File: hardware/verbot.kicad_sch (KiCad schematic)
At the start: 6 parts, among them J1 Raspberry Pi Zero 2 W, J2 5V USB power bank, M1 Pimoroni OnOff SHIM, M2 DRV8833 carrier, M3 Verbot 3V motor

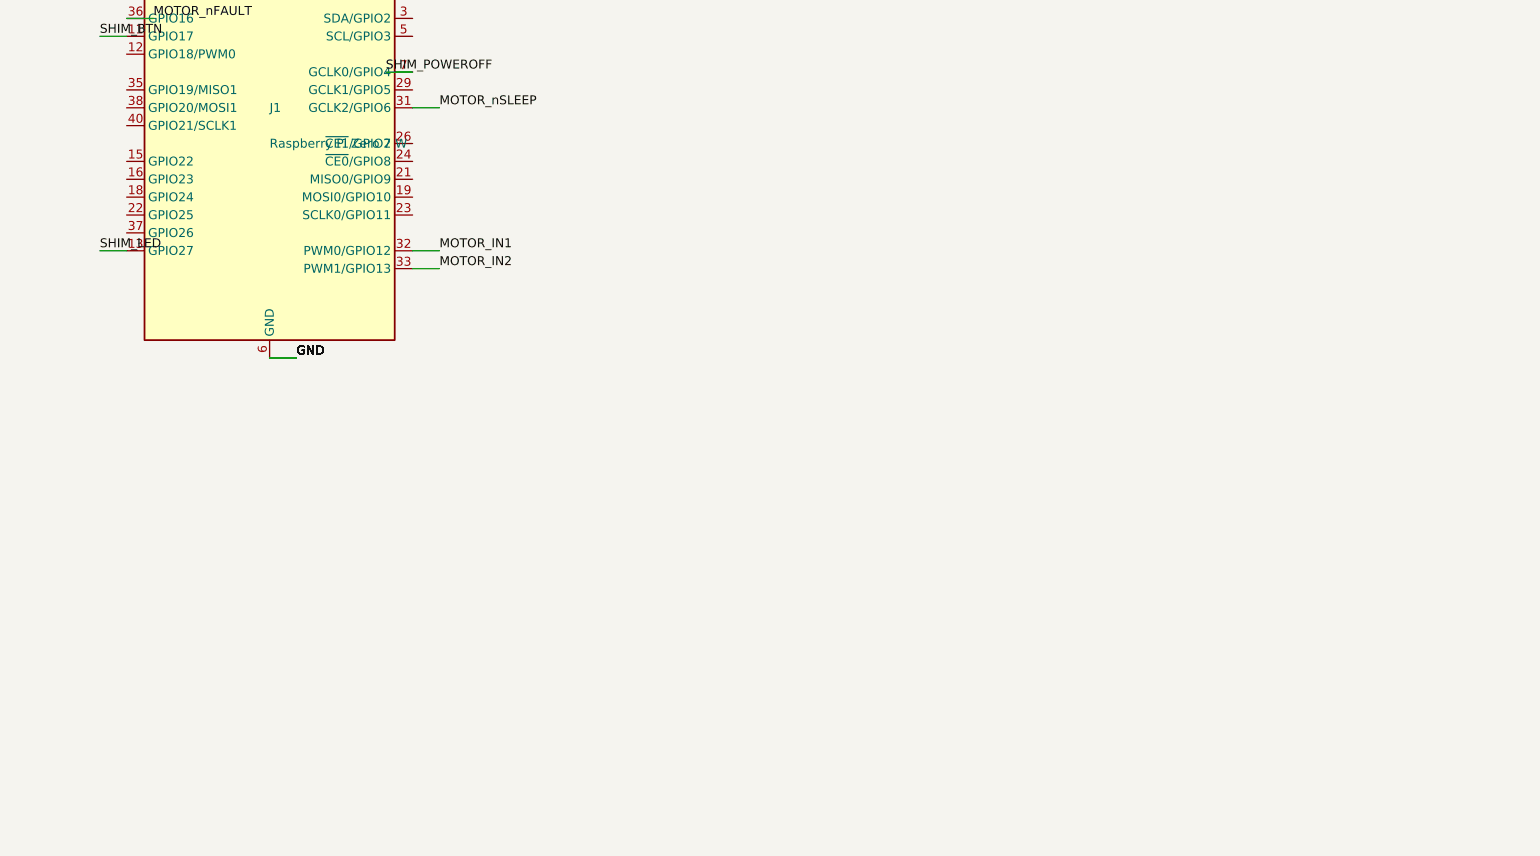
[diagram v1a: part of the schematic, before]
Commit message: feat(hardware): interrogation switch bank and limit switches
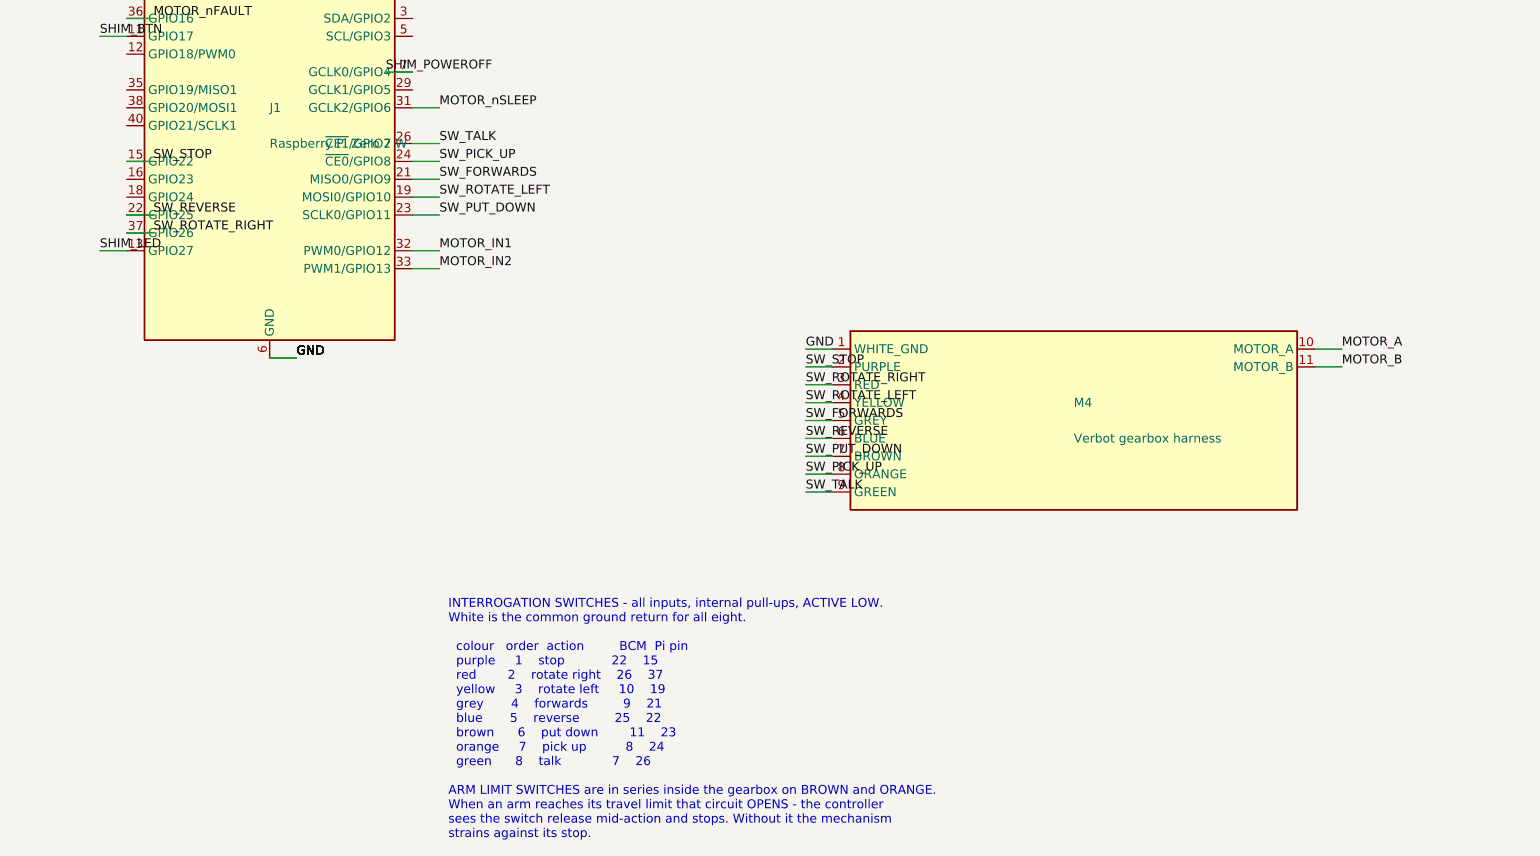
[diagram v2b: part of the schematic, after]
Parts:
- added M4: Verbot gearbox harness, symbol verbot:Verbot_Gearbox
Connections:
- net GND: now also M4.1 (WHITE_GND)
- net MOTOR_A: now also M4.10 (MOTOR_A)
- net MOTOR_B: now also M4.11 (MOTOR_B)
- net SW_STOP: now reaches J1.15 (GPIO22)
- net SW_STOP: now also M4.2 (PURPLE)
- net SW_ROTATE_LEFT: now reaches J1.19 (MOSI0/GPIO10)
- net SW_ROTATE_LEFT: now also M4.4 (YELLOW)
- net SW_FORWARDS: now reaches J1.21 (MISO0/GPIO9)
- net SW_FORWARDS: now also M4.5 (GREY)
- net SW_REVERSE: now reaches J1.22 (GPIO25)
- net SW_REVERSE: now also M4.6 (BLUE)
- net SW_PUT_DOWN: now reaches J1.23 (SCLK0/GPIO11)
- net SW_PUT_DOWN: now also M4.7 (BROWN)
- net SW_PICK_UP: now reaches J1.24 (~{CE0}/GPIO8)
- net SW_PICK_UP: now also M4.8 (ORANGE)
- net SW_TALK: now reaches J1.26 (~{CE1}/GPIO7)
- net SW_TALK: now also M4.9 (GREEN)
- net SW_ROTATE_RIGHT: now reaches J1.37 (GPIO26)
- net SW_ROTATE_RIGHT: now also M4.3 (RED)
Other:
- note added: "INTERROGATION SWITCHES - all inputs, internal pull-ups, ACTIVE LOW. White is the common ground return for all eight. colour order action BCM Pi pin purple 1 stop 22 15 red 2 rotate right 26 37 yellow 3 rotate left 10 19 grey 4 forwards 9 21 blue 5 reverse 25 22 brown 6 put down 11 23 orange 7 pick up 8 24 green 8 talk 7 26 ARM LIMIT SWITCHES are in series inside the gearbox on BROWN and ORANGE. W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"
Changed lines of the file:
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@@
 		(instances
 			(project "verbot"
-				(path "/607dc9e4-d310-4b00-b4a4-3bee0643b6b6" (reference "J1") (unit 1))))
+				(path "/7089de6d-abab-409e-9e27-515222eb95d8" (reference "J1") (unit 1))))
 	)
 	(symbol
@@
 		(instances
 			(project "verbot"
-				(path "/607dc9e4-d310-4b00-b4a4-3bee0643b6b6" (reference "M1") (unit 1))))
+				(path "/7089de6d-abab-409e-9e27-515222eb95d8" (reference "M1") (unit 1))))
 	)
 	(symbol
@@
 		(instances
 			(project "verbot"
-				(path "/607dc9e4-d310-4b00-b4a4-3bee0643b6b6" (reference "J2") (unit 1))))
+				(path "/7089de6d-abab-409e-9e27-515222eb95d8" (reference "J2") (unit 1))))
 	)
 	(wire (pts (xy 26.67 58.42) (xy 30.48 58.42))
@@
 		(instances
 			(project "verbot"
-				(path "/607dc9e4-d310-4b00-b4a4-3bee0643b6b6" (reference "#FLG01") (unit 1))))
+				(path "/7089de6d-abab-409e-9e27-515222eb95d8" (reference "#FLG01") (unit 1))))
 	)
 	(label "+5V" (at 44.45 105.41 0)
@@
 		(instances
 			(project "verbot"
-				(path "/607dc9e4-d310-4b00-b4a4-3bee0643b6b6" (reference "#FLG02") (unit 1))))
+				(path "/7089de6d-abab-409e-9e27-515222eb95d8" (reference "#FLG02") (unit 1))))
 	)
 	(label "+3V3" (at 69.85 105.41 0)
@@
 		(instances
 			(project "verbot"
-				(path "/607dc9e4-d310-4b00-b4a4-3bee0643b6b6" (reference "M2") (unit 1))))
+				(path "/7089de6d-abab-409e-9e27-515222eb95d8" (reference "M2") (unit 1))))
 	)
 	(symbol
@@
 		(instances
 			(project "verbot"
-				(path "/607dc9e4-d310-4b00-b4a4-3bee0643b6b6" (reference "M3") (unit 1))))
+				(path "/7089de6d-abab-409e-9e27-515222eb95d8" (reference "M3") (unit 1))))
 	)
 	(symbol
@@
 		(instances
 			(project "verbot"
-				(path "/607dc9e4-d310-4b00-b4a4-3bee0643b6b6" (reference "C1") (unit 1))))
+				(path "/7089de6d-abab-409e-9e27-515222eb95d8" (reference "C1") (unit 1))))
 	)
 	(wire (pts (xy 236.22 166.37) (xy 240.03 166.37))
@@
 	(text "MOTOR: only channel A is used.\nEEP may be tied to VCC by the carrier's J1 solder jumper - check with a\nmeter. If bridged, set VERBOT_MOTOR_SLEEP_PIN=null and BCM6 stays free.\nIf the motor runs backwards, swap OUT1/OUT2 rather than the code's sign\nconvention: interrogation must be the positive direction.\nVCC is the motor rail, NOT a logic rail - the 3V motor sees whatever it\nis fed. Never feed it from the Pi's 3V3 pin." (at 292.1 116.84 0)
 		(effects (font (size 1.27 1.27)) (justify left top)))
+	(symbol
+		(lib_id "verbot:Verbot_Gearbox")
+		(at 330.2 190.5 0)
+		(unit 1)
+		(exclude_from_sim no)
+		(in_bom yes)
+		(on_board yes)
+		(dnp no)
+		(property "Reference" "M4" (at 330.2 187.96 0)
+			(effects (font (size 1.27 1.27)) (justify left)))
+		(property "Value" "Verbot gearbox harness" (at 330.2 193.04 0)
+			(effects (font (size 1.27 1.27)) (justify left) ))
+		(pin "1")
+		(pin "2")
+		(pin "3")
+		(pin "4")
+		(pin "5")
+		(pin "6")
+		(pin "7")
+		(pin "8")
+		(pin "9")
+		(pin "10")
+		(pin "11")
+		(instances
+			(project "verbot"
+				(path "/7089de6d-abab-409e-9e27-515222eb95d8" (reference "M4") (unit 1))))
+	)
+	(wire (pts (xy 295.91 182.88) (xy 292.1 182.88))
+		(stroke (width 0) (type default)))
+	(label "SW_STOP" (at 292.1 182.88 0)
+		(effects (font (size 1.27 1.27)) (justify left bottom)))
+	(wire (pts (xy 195.58 153.67) (xy 199.39 153.67))
+		(stroke (width 0) (type default)))
+	(label "SW_STOP" (at 199.39 153.67 0)
+		(effects (font (size 1.27 1.27)) (justify left bottom)))
+	(wire (pts (xy 295.91 185.42) (xy 292.1 185.42))
+		(stroke (width 0) (type default)))
+	(label "SW_ROTATE_RIGHT" (at 292.1 185.42 0)
+		(effects (font (size 1.27 1.27)) (justify left bottom)))
+	(wire (pts (xy 195.58 163.83) (xy 199.39 163.83))
+		(stroke (width 0) (type default)))
+	(label "SW_ROTATE_RIGHT" (at 199.39 163.83 0)
+		(effects (font (size 1.27 1.27)) (justify left bottom)))
+	(wire (pts (xy 295.91 187.96) (xy 292.1 187.96))
+		(stroke (width 0) (type default)))
+	(label "SW_ROTATE_LEFT" (at 292.1 187.96 0)
+		(effects (font (size 1.27 1.27)) (justify left bottom)))
+	(wire (pts (xy 236.22 158.75) (xy 240.03 158.75))
+		(stroke (width 0) (type default)))
+	(label "SW_ROTATE_LEFT" (at 240.03 158.75 0)
+		(effects (font (size 1.27 1.27)) (justify left bottom)))
+	(wire (pts (xy 295.91 190.5) (xy 292.1 190.5))
+		(stroke (width 0) (type default)))
+	(label "SW_FORWARDS" (at 292.1 190.5 0)
+		(effects (font (size 1.27 1.27)) (justify left bottom)))
+	(wire (pts (xy 236.22 156.21) (xy 240.03 156.21))
+		(stroke (width 0) (type default)))
+	(label "SW_FORWARDS" (at 240.03 156.21 0)
+		(effects (font (size 1.27 1.27)) (justify left bottom)))
+	(wire (pts (xy 295.91 193.04) (xy 292.1 193.04))
+		(stroke (width 0) (type default)))
+	(label "SW_REVERSE" (at 292.1 193.04 0)
+		(effects (font (size 1.27 1.27)) (justify left bottom)))
+	(wire (pts (xy 195.58 161.29) (xy 199.39 161.29))
+		(stroke (width 0) (type default)))
+	(label "SW_REVERSE" (at 199.39 161.29 0)
+		(effects (font (size 1.27 1.27)) (justify left bottom)))
+	(wire (pts (xy 295.91 195.58) (xy 292.1 195.58))
+		(stroke (width 0) (type default)))
+	(label "SW_PUT_DOWN" (at 292.1 195.58 0)
+		(effects (font (size 1.27 1.27)) (justify left bottom)))
+	(wire (pts (xy 236.22 161.29) (xy 240.03 161.29))
+		(stroke (width 0) (type default)))
+	(label "SW_PUT_DOWN" (at 240.03 161.29 0)
+		(effects (font (size 1.27 1.27)) (justify left bottom)))
+	(wire (pts (xy 295.91 198.12) (xy 292.1 198.12))
+		(stroke (width 0) (type default)))
+	(label "SW_PICK_UP" (at 292.1 198.12 0)
+		(effects (font (size 1.27 1.27)) (justify left bottom)))
+	(wire (pts (xy 236.22 153.67) (xy 240.03 153.67))
+		(stroke (width 0) (type default)))
+	(label "SW_PICK_UP" (at 240.03 153.67 0)
+		(effects (font (size 1.27 1.27)) (justify left bottom)))
+	(wire (pts (xy 295.91 200.66) (xy 292.1 200.66))
+		(stroke (width 0) (type default)))
+	(label "SW_TALK" (at 292.1 200.66 0)
+		(effects (font (size 1.27 1.27)) (justify left bottom)))
+	(wire (pts (xy 236.22 151.13) (xy 240.03 151.13))
+		(stroke (width 0) (type default)))
+	(label "SW_TALK" (at 240.03 151.13 0)
+		(effects (font (size 1.27 1.27)) (justify left bottom)))
+	(wire (pts (xy 295.91 180.34) (xy 292.1 180.34))
+		(stroke (width 0) (type default)))
+	(label "GND" (at 292.1 180.34 0)
+		(effects (font (size 1.27 1.27)) (justify left bottom)))
+	(wire (pts (xy 364.49 180.34) (xy 368.3 180.34))
+		(stroke (width 0) (type default)))
+	(label "MOTOR_A" (at 368.3 180.34 0)
+		(effects (font (size 1.27 1.27)) (justify left bottom)))
+	(wire (pts (xy 364.49 182.88) (xy 368.3 182.88))
+		(stroke (width 0) (type default)))
+	(label "MOTOR_B" (at 368.3 182.88 0)
+		(effects (font (size 1.27 1.27)) (justify left bottom)))
+	(text "INTERROGATION SWITCHES - all inputs, internal pull-ups, ACTIVE LOW.\nWhite is the common ground return for all eight.\n\n  colour   order  action         BCM  Pi pin\n  purple     1    stop            22    15\n  red        2    rotate right    26    37\n  yellow     3    rotate left     10    19\n  grey       4    forwards         9    21\n  blue       5    reverse         25    22\n  brown      6    put down        11    23\n  orange     7    pick up          8    24\n  green      8    talk             7    26\n\nARM LIMIT SWITCHES are in series inside the gearbox on BROWN and ORANGE.\nWhen an arm reaches its travel limit that circuit OPENS - the controller\nsees the switch release mid-action and stops. Without it the mechanism\nstrains against its stop." (at 241.3 215.9 0)
+		(effects (font (size 1.27 1.27)) (justify left top)))
 	(sheet_instances
